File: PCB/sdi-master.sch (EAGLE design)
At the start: 21 parts, among them J4 POWER_JACKPTH_LOCK, U1 ATSAMD11C14A-SSUT, U3 LDL1117S12R

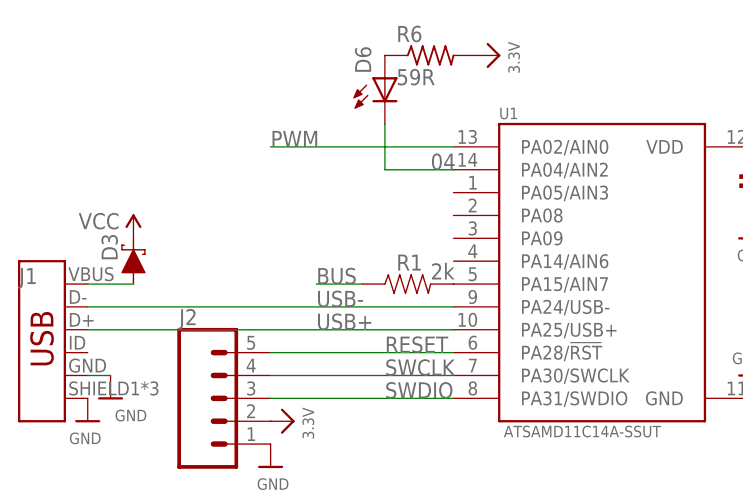
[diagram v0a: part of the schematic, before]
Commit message: added 4pin connector for remaining pins on all boards
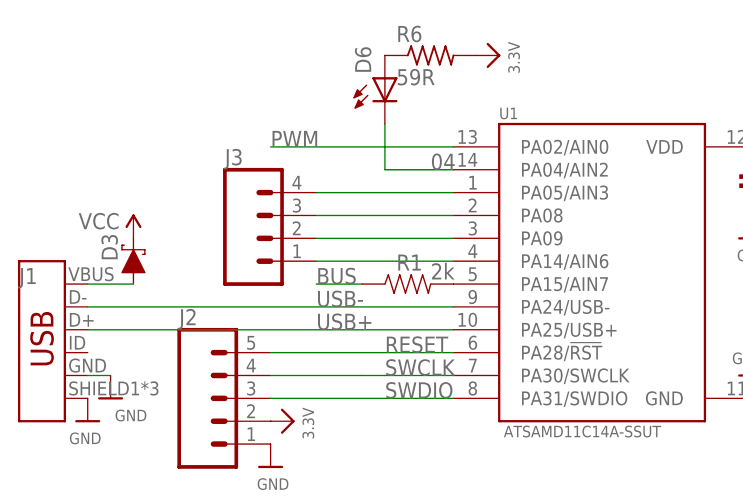
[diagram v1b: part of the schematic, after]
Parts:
- added J3: (no value), SparkFun-Connectors:CONN_04PTH
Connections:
- new net N$1: J3.4, U1.PA05/AIN3
- new net N$2: J3.3, U1.PA08
- new net N$3: J3.2, U1.PA09
- new net N$7: J3.1, U1.PA14/AIN6
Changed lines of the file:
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@@
 <?xml version="1.0" encoding="utf-8"?>
 <!DOCTYPE eagle SYSTEM "eagle.dtd">
-<eagle version="9.3.0">
+<eagle version="9.2.2">
 <drawing>
 <settings>
@@
 <part name="GND2" library="supply1" library_urn="urn:adsk.eagle:library:371" deviceset="GND" device=""/>
 <part name="J5" library="SparkFun-Connectors" library_urn="urn:adsk.eagle:library:513" deviceset="CONN_03" device="SCREW-NS" package3d_urn="urn:adsk.eagle:package:38088/1"/>
+<part name="J3" library="SparkFun-Connectors" deviceset="CONN_04" device="PTH"/>
 </parts>
 <sheets>
@@
 <attribute name="NAME" x="43.18" y="15.748" size="1.778" layer="95" font="vector" rot="MR0"/>
 </instance>
+<instance part="J3" gate="J1" x="-60.96" y="63.5" smashed="yes">
+<attribute name="VALUE" x="-66.04" y="56.134" size="1.778" layer="96" font="vector"/>
+<attribute name="NAME" x="-66.04" y="71.628" size="1.778" layer="95" font="vector"/>
+</instance>
 </instances>
 <busses>
@@
 </segment>
 </net>
+<net name="N$1" class="0">
+<segment>
+<pinref part="U1" gate="G$1" pin="PA05/AIN3"/>
+<pinref part="J3" gate="J1" pin="4"/>
+<wire x1="-40.64" y1="68.58" x2="-55.88" y2="68.58" width="0.1524" layer="91"/>
+</segment>
+</net>
+<net name="N$2" class="0">
+<segment>
+<pinref part="U1" gate="G$1" pin="PA08"/>
+<pinref part="J3" gate="J1" pin="3"/>
+<wire x1="-40.64" y1="66.04" x2="-55.88" y2="66.04" width="0.1524" layer="91"/>
+</segment>
+</net>
+<net name="N$3" class="0">
+<segment>
+<pinref part="U1" gate="G$1" pin="PA09"/>
+<pinref part="J3" gate="J1" pin="2"/>
+<wire x1="-40.64" y1="63.5" x2="-55.88" y2="63.5" width="0.1524" layer="91"/>
+</segment>
+</net>
+<net name="N$7" class="0">
+<segment>
+<pinref part="U1" gate="G$1" pin="PA14/AIN6"/>
+<pinref part="J3" gate="J1" pin="1"/>
+<wire x1="-40.64" y1="60.96" x2="-55.88" y2="60.96" width="0.1524" layer="91"/>
+</segment>
+</net>

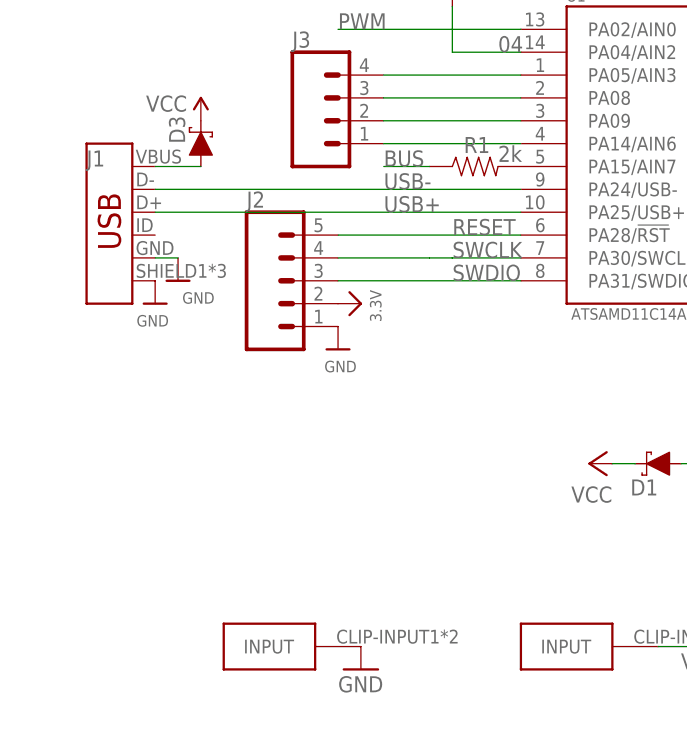
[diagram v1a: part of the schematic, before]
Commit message: modified sdi master to suit sdi application node
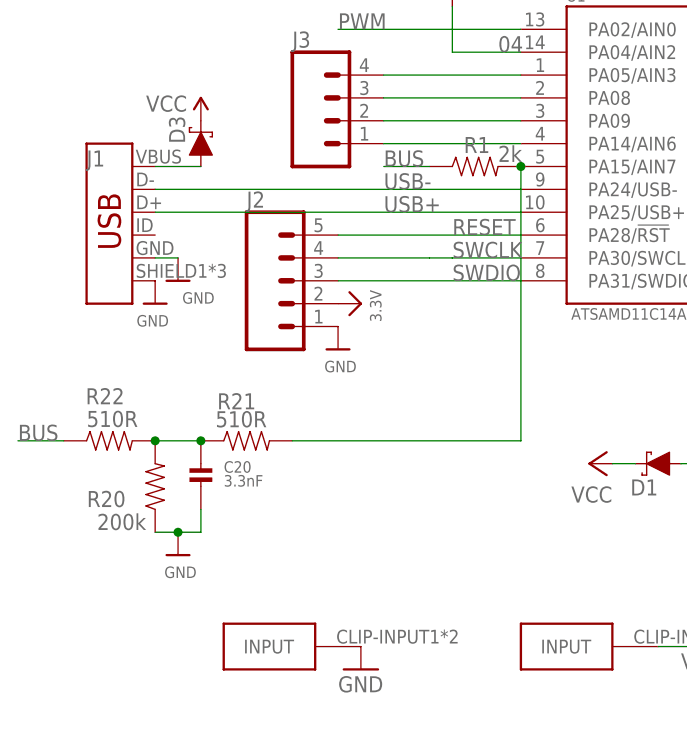
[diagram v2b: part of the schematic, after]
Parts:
- added C20: 3.3nF, microbuilder:CAP_CERAMIC0603
- added R20: 200k, SparkFun-Resistors:RESISTOR1206
- added R21, R22: 510R, SparkFun-Resistors:RESISTOR1206
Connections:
- new net N$8: C20.P$1, R20.2, R21.1, R22.2
- net BUS: now also R22.1
- net GND: now also C20.P$2, R20.1
- net N$5: now also R21.2
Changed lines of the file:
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@@
 <setting verticaltext="up"/>
 </settings>
-<grid distance="0.1" unitdist="inch" unit="inch" style="lines" multiple="1" display="no" altdistance="0.01" altunitdist="inch" altunit="inch"/>
+<grid distance="1" unitdist="mm" unit="mm" style="lines" multiple="1" display="no" altdistance="0.01" altunitdist="inch" altunit="inch"/>
 <layers>
 <layer number="1" name="Top" color="4" fill="1" visible="no" active="no"/>
@@
 <part name="J5" library="SparkFun-Connectors" library_urn="urn:adsk.eagle:library:513" deviceset="CONN_03" device="SCREW-NS" package3d_urn="urn:adsk.eagle:package:38088/1"/>
 <part name="J3" library="SparkFun-Connectors" deviceset="CONN_04" device="PTH"/>
+<part name="R21" library="SparkFun-Resistors" deviceset="RESISTOR" device="1206" value="510R"/>
+<part name="R22" library="SparkFun-Resistors" deviceset="RESISTOR" device="1206" value="510R"/>
+<part name="C20" library="microbuilder" deviceset="CAP_CERAMIC" device="0603" value="3.3nF"/>
+<part name="R20" library="SparkFun-Resistors" deviceset="RESISTOR" device="1206" value="200k"/>
+<part name="U$11" library="microbuilder" deviceset="GND" device=""/>
 </parts>
 <sheets>
@@
 <attribute name="NAME" x="-66.04" y="71.628" size="1.778" layer="95" font="vector"/>
 </instance>
+<instance part="R21" gate="G$1" x="-71.12" y="27.94" smashed="yes">
+<attribute name="NAME" x="-74.39" y="31.4386" size="1.778" layer="95"/>
+<attribute name="VALUE" x="-74.58" y="29.448" size="1.778" layer="96"/>
+</instance>
+<instance part="R22" gate="G$1" x="-86.36" y="27.94" smashed="yes">
+<attribute name="NAME" x="-89" y="32" size="1.778" layer="95"/>
+<attribute name="VALUE" x="-88.9" y="29.48" size="1.778" layer="96"/>
+</instance>
+<instance part="C20" gate="G$1" x="-76.2" y="22.86" smashed="yes">
+<attribute name="NAME" x="-73.66" y="24.4" size="1.27" layer="95" font="vector"/>
+<attribute name="VALUE" x="-73.66" y="22.86" size="1.27" layer="96" font="vector"/>
+</instance>
+<instance part="R20" gate="G$1" x="-81.28" y="22.86" smashed="yes" rot="R90">
+<attribute name="NAME" x="-84.55" y="22.3614" size="1.778" layer="95" rot="R180"/>
+<attribute name="VALUE" x="-82.28" y="19.812" size="1.778" layer="96" rot="R180"/>
+</instance>
+<instance part="U$11" gate="G$1" x="-78.74" y="15.24" smashed="yes">
+<attribute name="VALUE" x="-80.264" y="12.7" size="1.27" layer="96"/>
+</instance>
 </instances>
 <busses>
@@
 <pinref part="J5" gate="J$1" pin="1"/>
 <pinref part="GND1" gate="1" pin="GND"/>
+</segment>
+<segment>
+<pinref part="R20" gate="G$1" pin="1"/>
+<pinref part="U$11" gate="G$1" pin="GND"/>
+<wire x1="-81.28" y1="17.78" x2="-78.74" y2="17.78" width="0.1524" layer="91"/>
+<pinref part="C20" gate="G$1" pin="P$2"/>
+<wire x1="-78.74" y1="17.78" x2="-76.2" y2="17.78" width="0.1524" layer="91"/>
+<wire x1="-76.2" y1="17.78" x2="-76.2" y2="20.32" width="0.1524" layer="91"/>
+<junction x="-78.74" y="17.78"/>
 </segment>
 </net>
@@
 <pinref part="U1" gate="G$1" pin="PA15/AIN7"/>
 <pinref part="R1" gate="G$1" pin="2"/>
+<wire x1="-40.64" y1="58.42" x2="-40.64" y2="27.94" width="0.1524" layer="91"/>
+<junction x="-40.64" y="58.42"/>
+<wire x1="-40.64" y1="27.94" x2="-66.04" y2="27.94" width="0.1524" layer="91"/>
+<pinref part="R21" gate="G$1" pin="2"/>
 </segment>
 </net>
@@
 <pinref part="J5" gate="J$1" pin="2"/>
 <wire x1="33.02" y1="10.16" x2="20.32" y2="10.16" width="0.1524" layer="91"/>
+</segment>
+<segment>
+<pinref part="R22" gate="G$1" pin="1"/>
+<wire x1="-91.44" y1="27.94" x2="-96.52" y2="27.94" width="0.1524" layer="91"/>
+<label x="-96.52" y="27.94" size="1.778" layer="95"/>
 </segment>
 </net>
@@
 </segment>
 </net>
+<net name="N$8" class="0">
+<segment>
+<pinref part="R21" gate="G$1" pin="1"/>
+<pinref part="R22" gate="G$1" pin="2"/>
+<wire x1="-76.2" y1="27.94" x2="-81.28" y2="27.94" width="0.1524" layer="91"/>
+<pinref part="C20" gate="G$1" pin="P$1"/>
+<junction x="-76.2" y="27.94"/>
+<pinref part="R20" gate="G$1" pin="2"/>
+<junction x="-81.28" y="27.94"/>
+</segment>
+</net>
